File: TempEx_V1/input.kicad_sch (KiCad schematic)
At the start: 6 parts, among them J1 Conn_01x02, U1 MAX31865xTP

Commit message: WIP
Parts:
- C1, C2: footprint (none) -> Capacitor_SMD:C_0603_1608Metric_Pad1.08x0.95mm_HandSolder
- C9: value (none) -> 100n; footprint (none) -> Capacitor_SMD:C_0603_1608Metric_Pad1.08x0.95mm_HandSolder
- J1: footprint (none) -> Connector_Molex:Molex_SL_171971-0002_1x02_P2.54mm_Vertical
- R1: value (none) -> 400; footprint (none) -> Resistor_SMD:R_0201_0603Metric_Pad0.64x0.40mm_HandSolder
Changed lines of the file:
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@@
   (junction (at 134.62 96.266) (diameter 0) (color 0 0 0 0)
   )
-  (junction (at 179.578 73.66) (diameter 0) (color 0 0 0 0)
-  )
   (junction (at 204.978 100.584) (diameter 0) (color 0 0 0 0)
   )
@@
   )
   (junction (at 209.296 100.584) (diameter 0) (color 0 0 0 0)
+  )
+  (junction (at 177.038 73.66) (diameter 0) (color 0 0 0 0)
   )
   (no_connect (at 164.338 81.788))
@@
     (stroke (width 0) (type default) (color 0 0 0 0))
   )
-  (wire (pts (xy 179.578 71.628) (xy 179.578 73.66))
+  (wire (pts (xy 177.038 71.628) (xy 177.038 73.66))
     (stroke (width 0) (type default) (color 0 0 0 0))
   )
@@
     (stroke (width 0) (type default) (color 0 0 0 0))
   )
-  (wire (pts (xy 179.578 73.66) (xy 177.038 73.66))
-    (stroke (width 0) (type default) (color 0 0 0 0))
-  )
   (wire (pts (xy 197.358 81.788) (xy 200.152 81.788))
     (stroke (width 0) (type default) (color 0 0 0 0))
@@
     (stroke (width 0) (type default) (color 0 0 0 0))
   )
-  (wire (pts (xy 182.118 73.66) (xy 179.578 73.66))
+  (wire (pts (xy 177.038 73.66) (xy 182.118 73.66))
     (stroke (width 0) (type default) (color 0 0 0 0))
   )
@@
     (effects (font (size 1.27 1.27)) (justify right))
   )
-  (symbol (lib_id "power:+3.3V") (at 179.578 71.628 0) (mirror y) (unit 1)
+  (symbol (lib_id "power:+3.3V") (at 177.038 71.628 0) (mirror y)
     (in_bom yes) (on_board yes) (fields_autoplaced)
-    (property "Reference" "#PWR06" (id 0) (at 179.578 75.438 0)
-      (effects (font (size 1.27 1.27)) hide)
-    )
-    (property "Value" "" (id 1) (at 179.578 66.548 0))
-    (property "Footprint" "" (id 2) (at 179.578 71.628 0)
-      (effects (font (size 1.27 1.27)) hide)
-    )
-    (property "Datasheet" "" (id 3) (at 179.578 71.628 0)
-      (effects (font (size 1.27 1.27)) hide)
-    )
-    (pin "1")
-  )
-  (symbol (lib_id "power:GND") (at 137.16 106.934 0) (mirror y) (unit 1)
-    (in_bom yes) (on_board yes)
-    (property "Reference" "#PWR02" (id 0) (at 137.16 113.284 0)
+    (property "Reference" "#PWR024" (id 0) (at 177.038 75.438 0)
+      (effects (font (size 1.27 1.27)) hide)
+    )
+    (property "Value" "+3.3V" (id 1) (at 177.038 66.548 0))
+    (property "Footprint" "" (id 2) (at 177.038 71.628 0)
+      (effects (font (size 1.27 1.27)) hide)
+    )
+    (property "Datasheet" "" (id 3) (at 177.038 71.628 0)
+      (effects (font (size 1.27 1.27)) hide)
+    )
+    (pin "1")
+  )
+  (symbol (lib_id "power:GND") (at 137.16 106.934 0) (mirror y)
+    (in_bom yes) (on_board yes)
+    (property "Reference" "#PWR020" (id 0) (at 137.16 113.284 0)
       (effects (font (size 1.27 1.27)) hide)
     )
@@
     (pin "1")
   )
-  (symbol (lib_id "Sensor_Temperature:MAX31865xTP") (at 179.578 97.028 0) (unit 1)
+  (symbol (lib_id "Sensor_Temperature:MAX31865xTP") (at 179.578 97.028 0)
     (in_bom yes) (on_board yes) (fields_autoplaced)
     (property "Reference" "U1" (id 0) (at 174.2693 73.406 0)
@@
     (pin "9")
   )
-  (symbol (lib_id "Device:C") (at 204.978 104.394 0) (mirror y) (unit 1)
+  (symbol (lib_id "Device:C") (at 204.978 104.394 0) (mirror y)
     (in_bom yes) (on_board yes)
     (property "Reference" "C9" (id 0) (at 204.216 102.108 0)
       (effects (font (size 1.27 1.27)) (justify left))
     )
-    (property "Value" "" (id 1) (at 204.216 106.68 0)
-      (effects (font (size 1.27 1.27)) (justify left))
-    )
-    (property "Footprint" "" (id 2) (at 204.0128 108.204 0)
+    (property "Value" "100n" (id 1) (at 204.216 106.68 0)
+      (effects (font (size 1.27 1.27)) (justify left))
+    )
+    (property "Footprint" "Capacitor_SMD:C_0603_1608Metric_Pad1.08x0.95mm_HandSolder" (id 2) (at 204.0128 108.204 0)
       (effects (font (size 1.27 1.27)) hide)
     )
@@
     (pin "2")
   )
-  (symbol (lib_id "Device:C") (at 137.16 103.124 0) (mirror y) (unit 1)
+  (symbol (lib_id "Device:C") (at 137.16 103.124 0) (mirror y)
     (in_bom yes) (on_board yes)
     (property "Reference" "C1" (id 0) (at 140.716 100.838 0)
@@
       (effects (font (size 1.27 1.27)) (justify left))
     )
-    (property "Footprint" "" (id 2) (at 136.1948 106.934 0)
+    (property "Footprint" "Capacitor_SMD:C_0603_1608Metric_Pad1.08x0.95mm_HandSolder" (id 2) (at 136.1948 106.934 0)
       (effects (font (size 1.27 1.27)) hide)
     )
@@
     (pin "2")
   )
-  (symbol (lib_id "Device:C") (at 132.08 103.124 0) (mirror y) (unit 1)
+  (symbol (lib_id "Device:C") (at 132.08 103.124 0) (mirror y)
     (in_bom yes) (on_board yes)
     (property "Reference" "C2" (id 0) (at 131.572 100.838 0)
@@
       (effects (font (size 1.27 1.27)) (justify left))
     )
-    (property "Footprint" "" (id 2) (at 131.1148 106.934 0)
+    (property "Footprint" "Capacitor_SMD:C_0603_1608Metric_Pad1.08x0.95mm_HandSolder" (id 2) (at 131.1148 106.934 0)
       (effects (font (size 1.27 1.27)) hide)
     )
@@
     (pin "2")
   )
-  (symbol (lib_id "power:GND") (at 196.85 95.25 0) (mirror y) (unit 1)
-    (in_bom yes) (on_board yes)
-    (property "Reference" "#PWR026" (id 0) (at 196.85 101.6 0)
+  (symbol (lib_id "power:GND") (at 196.85 95.25 0) (mirror y)
+    (in_bom yes) (on_board yes)
+    (property "Reference" "#PWR029" (id 0) (at 196.85 101.6 0)
       (effects (font (size 1.27 1.27)) hide)
     )
@@
     (pin "1")
   )
-  (symbol (lib_id "power:GND") (at 182.118 114.808 0) (mirror y) (unit 1)
-    (in_bom yes) (on_board yes)
-    (property "Reference" "#PWR05" (id 0) (at 182.118 121.158 0)
+  (symbol (lib_id "power:PWR_FLAG") (at 182.118 73.66 0)
+    (in_bom yes) (on_board yes)
+    (property "Reference" "#FLG0104" (id 0) (at 182.118 71.755 0)
+      (effects (font (size 1.27 1.27)) hide)
+    )
+    (property "Value" "PWR_FLAG" (id 1) (at 186.563 69.977 0))
+    (property "Footprint" "" (id 2) (at 182.118 73.66 0)
+      (effects (font (size 1.27 1.27)) hide)
+    )
+    (property "Datasheet" "~" (id 3) (at 182.118 73.66 0)
+      (effects (font (size 1.27 1.27)) hide)
+    )
+    (pin "1")
+  )
+  (symbol (lib_id "power:GND") (at 182.118 114.808 0) (mirror y)
+    (in_bom yes) (on_board yes)
+    (property "Reference" "#PWR023" (id 0) (at 182.118 121.158 0)
       (effects (font (size 1.27 1.27)) hide)
     )
@@
     (pin "1")
   )
-  (symbol (lib_id "power:GNDD") (at 132.08 106.934 0) (mirror y) (unit 1)
-    (in_bom yes) (on_board yes)
-    (property "Reference" "#PWR04" (id 0) (at 132.08 113.284 0)
+  (symbol (lib_id "power:GNDD") (at 132.08 106.934 0) (mirror y)
+    (in_bom yes) (on_board yes)
+    (property "Reference" "#PWR022" (id 0) (at 132.08 113.284 0)
       (effects (font (size 1.27 1.27)) hide)
     )
@@
     (pin "1")
   )
-  (symbol (lib_id "Connector_Generic:Conn_01x02") (at 214.376 103.378 0) (unit 1)
+  (symbol (lib_id "Connector_Generic:Conn_01x02") (at 214.376 103.378 0)
     (in_bom yes) (on_board yes) (fields_autoplaced)
     (property "Reference" "J1" (id 0) (at 216.408 103.3779 0)
@@
       (effects (font (size 1.27 1.27)) (justify left))
     )
-    (property "Footprint" "" (id 2) (at 214.376 103.378 0)
+    (property "Footprint" "Connector_Molex:Molex_SL_171971-0002_1x02_P2.54mm_Vertical" (id 2) (at 214.376 103.378 0)
       (effects (font (size 1.27 1.27)) hide)
     )
@@
     (pin "2")
   )
-  (symbol (lib_id "power:GNDD") (at 177.038 114.808 0) (mirror y) (unit 1)
-    (in_bom yes) (on_board yes)
-    (property "Reference" "#PWR07" (id 0) (at 177.038 121.158 0)
+  (symbol (lib_id "power:GNDD") (at 177.038 114.808 0) (mirror y)
+    (in_bom yes) (on_board yes)
+    (property "Reference" "#PWR025" (id 0) (at 177.038 121.158 0)
       (effects (font (size 1.27 1.27)) hide)
     )
@@
     (pin "1")
   )
-  (symbol (lib_id "power:+3.3V") (at 134.62 94.234 0) (mirror y) (unit 1)
+  (symbol (lib_id "power:+3.3V") (at 134.62 94.234 0) (mirror y)
     (in_bom yes) (on_board yes) (fields_autoplaced)
-    (property "Reference" "#PWR03" (id 0) (at 134.62 98.044 0)
-      (effects (font (size 1.27 1.27)) hide)
-    )
-    (property "Value" "" (id 1) (at 134.62 88.646 0))
+    (property "Reference" "#PWR021" (id 0) (at 134.62 98.044 0)
+      (effects (font (size 1.27 1.27)) hide)
+    )
+    (property "Value" "+3.3V" (id 1) (at 134.62 88.646 0))
     (property "Footprint" "" (id 2) (at 134.62 94.234 0)
       (effects (font (size 1.27 1.27)) hide)
@@
     (pin "1")
   )
-  (symbol (lib_id "Device:R") (at 200.152 85.598 0) (unit 1)
+  (symbol (lib_id "Device:R") (at 200.152 85.598 0)
     (in_bom yes) (on_board yes)
     (property "Reference" "R1" (id 0) (at 201.93 84.582 0)
       (effects (font (size 1.27 1.27)) (justify left))
     )
-    (property "Value" "" (id 1) (at 201.676 86.614 0)
-      (effects (font (size 1.27 1.27)) (justify left))
-    )
-    (property "Footprint" "" (id 2) (at 198.374 85.598 90)
-      (effects (font (size 1.27 1.27)) hide)
-    )
+    (property "Value" "400" (id 1) (at 201.676 86.614 0)
+      (effects (font (size 1.27 1.27)) (justify left))
+    )
+    (property "Footprint" "Resistor_SMD:R_0201_0603Metric_Pad0.64x0.40mm_HandSolder" (id 2) (at 198.374 85.598 90)
+      (effects (font (size 1.27 1.27)) hide)
+    )

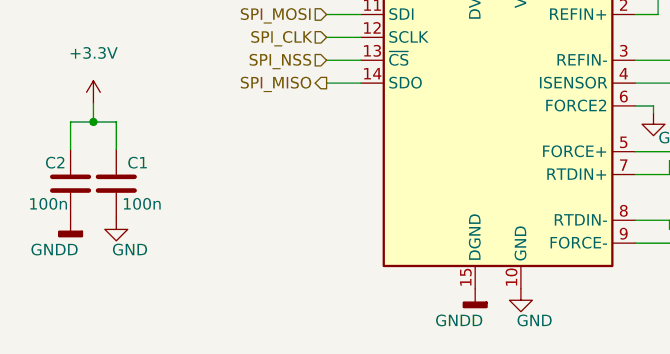
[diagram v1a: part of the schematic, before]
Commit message: GNDD Problem still unresolved
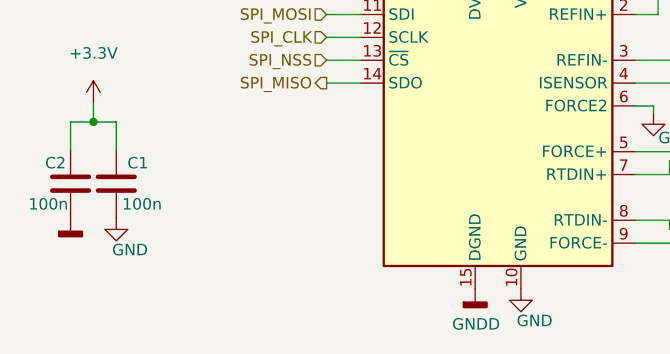
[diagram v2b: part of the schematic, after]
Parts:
- R1: footprint Resistor_SMD:R_0201_0603Metric_Pad0.64x0.40mm_HandSolder -> (none)
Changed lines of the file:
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@@
     (effects (font (size 1.27 1.27)) (justify right))
   )
-  (symbol (lib_id "power:+3.3V") (at 177.038 71.628 0) (mirror y)
-    (in_bom yes) (on_board yes) (fields_autoplaced)
-    (property "Reference" "#PWR024" (id 0) (at 177.038 75.438 0)
+  (symbol (lib_id "power:+3.3V") (at 177.038 71.628 0) (mirror y) (unit 1)
+    (in_bom yes) (on_board yes) (fields_autoplaced)
+    (property "Reference" "#PWR06" (id 0) (at 177.038 75.438 0)
       (effects (font (size 1.27 1.27)) hide)
     )
@@
     (pin "1")
   )
-  (symbol (lib_id "power:GND") (at 137.16 106.934 0) (mirror y)
-    (in_bom yes) (on_board yes)
-    (property "Reference" "#PWR020" (id 0) (at 137.16 113.284 0)
+  (symbol (lib_id "power:GNDD") (at 132.08 106.934 0) (unit 1)
+    (in_bom yes) (on_board yes)
+    (property "Reference" "#PWR022" (id 0) (at 132.08 113.284 0)
+      (effects (font (size 1.27 1.27)) hide)
+    )
+    (property "Value" "" (id 1) (at 132.1816 110.871 0))
+    (property "Footprint" "" (id 2) (at 132.08 106.934 0)
+      (effects (font (size 1.27 1.27)) hide)
+    )
+    (property "Datasheet" "" (id 3) (at 132.08 106.934 0)
+      (effects (font (size 1.27 1.27)) hide)
+    )
+    (pin "1")
+  )
+  (symbol (lib_id "power:GND") (at 137.16 106.934 0) (mirror y) (unit 1)
+    (in_bom yes) (on_board yes)
+    (property "Reference" "#PWR02" (id 0) (at 137.16 113.284 0)
       (effects (font (size 1.27 1.27)) hide)
     )
@@
     (pin "1")
   )
-  (symbol (lib_id "Sensor_Temperature:MAX31865xTP") (at 179.578 97.028 0)
+  (symbol (lib_id "Sensor_Temperature:MAX31865xTP") (at 179.578 97.028 0) (unit 1)
     (in_bom yes) (on_board yes) (fields_autoplaced)
     (property "Reference" "U1" (id 0) (at 174.2693 73.406 0)
@@
     (pin "9")
   )
-  (symbol (lib_id "Device:C") (at 204.978 104.394 0) (mirror y)
+  (symbol (lib_id "Device:C") (at 204.978 104.394 0) (mirror y) (unit 1)
     (in_bom yes) (on_board yes)
     (property "Reference" "C9" (id 0) (at 204.216 102.108 0)
@@
     (pin "2")
   )
-  (symbol (lib_id "Device:C") (at 137.16 103.124 0) (mirror y)
+  (symbol (lib_id "Device:C") (at 137.16 103.124 0) (mirror y) (unit 1)
     (in_bom yes) (on_board yes)
     (property "Reference" "C1" (id 0) (at 140.716 100.838 0)
@@
     (pin "2")
   )
-  (symbol (lib_id "Device:C") (at 132.08 103.124 0) (mirror y)
+  (symbol (lib_id "Device:C") (at 132.08 103.124 0) (mirror y) (unit 1)
     (in_bom yes) (on_board yes)
     (property "Reference" "C2" (id 0) (at 131.572 100.838 0)
@@
     (pin "2")
   )
-  (symbol (lib_id "power:GND") (at 196.85 95.25 0) (mirror y)
-    (in_bom yes) (on_board yes)
-    (property "Reference" "#PWR029" (id 0) (at 196.85 101.6 0)
+  (symbol (lib_id "power:GNDD") (at 177.038 114.808 0) (unit 1)
+    (in_bom yes) (on_board yes)
+    (property "Reference" "#PWR07" (id 0) (at 177.038 121.158 0)
+      (effects (font (size 1.27 1.27)) hide)
+    )
+    (property "Value" "GNDD" (id 1) (at 177.1396 118.745 0))
+    (property "Footprint" "" (id 2) (at 177.038 114.808 0)
+      (effects (font (size 1.27 1.27)) hide)
+    )
+    (property "Datasheet" "" (id 3) (at 177.038 114.808 0)
+      (effects (font (size 1.27 1.27)) hide)
+    )
+    (pin "1")
+  )
+  (symbol (lib_id "power:GND") (at 196.85 95.25 0) (mirror y) (unit 1)
+    (in_bom yes) (on_board yes)
+    (property "Reference" "#PWR026" (id 0) (at 196.85 101.6 0)
       (effects (font (size 1.27 1.27)) hide)
     )
@@
     (pin "1")
   )
-  (symbol (lib_id "power:PWR_FLAG") (at 182.118 73.66 0)
-    (in_bom yes) (on_board yes)
-    (property "Reference" "#FLG0104" (id 0) (at 182.118 71.755 0)
+  (symbol (lib_id "power:PWR_FLAG") (at 182.118 73.66 0) (unit 1)
+    (in_bom yes) (on_board yes)
+    (property "Reference" "#FLG0101" (id 0) (at 182.118 71.755 0)
       (effects (font (size 1.27 1.27)) hide)
     )
@@
     (pin "1")
   )
-  (symbol (lib_id "power:GND") (at 182.118 114.808 0) (mirror y)
-    (in_bom yes) (on_board yes)
-    (property "Reference" "#PWR023" (id 0) (at 182.118 121.158 0)
+  (symbol (lib_id "power:GND") (at 182.118 114.808 0) (mirror y) (unit 1)
+    (in_bom yes) (on_board yes)
+    (property "Reference" "#PWR05" (id 0) (at 182.118 121.158 0)
       (effects (font (size 1.27 1.27)) hide)
     )
@@
     (pin "1")
   )
-  (symbol (lib_id "power:GNDD") (at 132.08 106.934 0) (mirror y)
-    (in_bom yes) (on_board yes)
-    (property "Reference" "#PWR022" (id 0) (at 132.08 113.284 0)
-      (effects (font (size 1.27 1.27)) hide)
-    )
-    (property "Value" "GNDD" (id 1) (at 130.302 110.49 0))
-    (property "Footprint" "" (id 2) (at 132.08 106.934 0)
-      (effects (font (size 1.27 1.27)) hide)
-    )
-    (property "Datasheet" "" (id 3) (at 132.08 106.934 0)
-      (effects (font (size 1.27 1.27)) hide)
-    )
-    (pin "1")
-  )
-  (symbol (lib_id "Connector_Generic:Conn_01x02") (at 214.376 103.378 0)
+  (symbol (lib_id "Connector_Generic:Conn_01x02") (at 214.376 103.378 0) (unit 1)
     (in_bom yes) (on_board yes) (fields_autoplaced)
     (property "Reference" "J1" (id 0) (at 216.408 103.3779 0)
@@
     (pin "2")
   )
-  (symbol (lib_id "power:GNDD") (at 177.038 114.808 0) (mirror y)
-    (in_bom yes) (on_board yes)
-    (property "Reference" "#PWR025" (id 0) (at 177.038 121.158 0)
-      (effects (font (size 1.27 1.27)) hide)
-    )
-    (property "Value" "GNDD" (id 1) (at 175.26 118.364 0))
-    (property "Footprint" "" (id 2) (at 177.038 114.808 0)
-      (effects (font (size 1.27 1.27)) hide)
-    )
-    (property "Datasheet" "" (id 3) (at 177.038 114.808 0)
-      (effects (font (size 1.27 1.27)) hide)
-    )
-    (pin "1")
-  )
-  (symbol (lib_id "power:+3.3V") (at 134.62 94.234 0) (mirror y)
-    (in_bom yes) (on_board yes) (fields_autoplaced)
-    (property "Reference" "#PWR021" (id 0) (at 134.62 98.044 0)
+  (symbol (lib_id "power:+3.3V") (at 134.62 94.234 0) (mirror y) (unit 1)
+    (in_bom yes) (on_board yes) (fields_autoplaced)
+    (property "Reference" "#PWR03" (id 0) (at 134.62 98.044 0)
       (effects (font (size 1.27 1.27)) hide)
     )
@@
     (pin "1")
   )
-  (symbol (lib_id "Device:R") (at 200.152 85.598 0)
+  (symbol (lib_id "Device:R") (at 200.152 85.598 0) (unit 1)
     (in_bom yes) (on_board yes)
     (property "Reference" "R1" (id 0) (at 201.93 84.582 0)
@@
       (effects (font (size 1.27 1.27)) (justify left))
     )
-    (property "Footprint" "Resistor_SMD:R_0201_0603Metric_Pad0.64x0.40mm_HandSolder" (id 2) (at 198.374 85.598 90)
-      (effects (font (size 1.27 1.27)) hide)
-    )
+    (property "Footprint" "" (id 2) (at 198.374 85.598 90)
+      (effects (font (size 1.27 1.27)) hide)
+    )

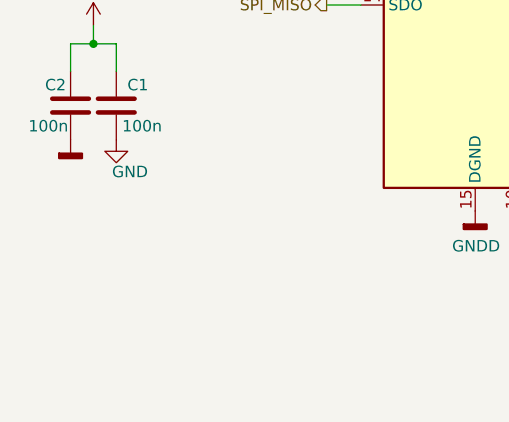
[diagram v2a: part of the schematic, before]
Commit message: Stitching missing
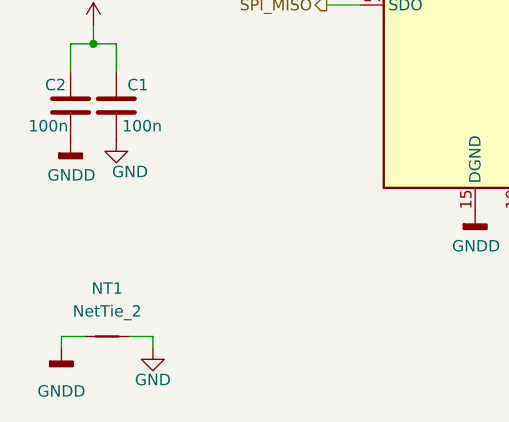
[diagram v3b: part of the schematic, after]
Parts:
- added NT1: NetTie_2, symbol Device:NetTie_2
- R1: footprint (none) -> Resistor_SMD:R_0603_1608Metric_Pad0.98x0.95mm_HandSolder
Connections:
- net GND: now also NT1.2
- net GNDD: now also NT1.1
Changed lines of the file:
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@@
+    (stroke (width 0) (type default) (color 0 0 0 0))
+  )
+  (wire (pts (xy 138.684 128.778) (xy 141.224 128.778))
     (stroke (width 0) (type default) (color 0 0 0 0))
   )
@@
     (stroke (width 0) (type default) (color 0 0 0 0))
   )
+  (wire (pts (xy 141.224 128.778) (xy 141.224 130.048))
+    (stroke (width 0) (type default) (color 0 0 0 0))
+  )
   (wire (pts (xy 194.818 81.788) (xy 197.358 81.788))
     (stroke (width 0) (type default) (color 0 0 0 0))
@@
     (stroke (width 0) (type default) (color 0 0 0 0))
   )
+  (wire (pts (xy 131.064 130.048) (xy 131.064 128.778))
+    (stroke (width 0) (type default) (color 0 0 0 0))
+  )
   (wire (pts (xy 177.038 71.628) (xy 177.038 73.66))
     (stroke (width 0) (type default) (color 0 0 0 0))
@@
   )
   (wire (pts (xy 194.818 94.488) (xy 196.85 94.488))
+    (stroke (width 0) (type default) (color 0 0 0 0))
+  )
+  (wire (pts (xy 131.064 128.778) (xy 133.604 128.778))
     (stroke (width 0) (type default) (color 0 0 0 0))
   )
@@
       (effects (font (size 1.27 1.27)) hide)
     )
-    (property "Value" "" (id 1) (at 132.1816 110.871 0))
+    (property "Value" "GNDD" (id 1) (at 132.1816 110.871 0))
     (property "Footprint" "" (id 2) (at 132.08 106.934 0)
       (effects (font (size 1.27 1.27)) hide)
@@
     (pin "1")
   )
+  (symbol (lib_id "Device:NetTie_2") (at 136.144 128.778 0) (unit 1)
+    (in_bom yes) (on_board yes) (fields_autoplaced)
+    (property "Reference" "NT1" (id 0) (at 136.144 123.444 0))
+    (property "Value" "NetTie_2" (id 1) (at 136.144 125.984 0))
+    (property "Footprint" "" (id 2) (at 136.144 128.778 0)
+      (effects (font (size 1.27 1.27)) hide)
+    )
+    (property "Datasheet" "~" (id 3) (at 136.144 128.778 0)
+      (effects (font (size 1.27 1.27)) hide)
+    )
+    (pin "1")
+    (pin "2")
+  )
   (symbol (lib_id "power:GND") (at 196.85 95.25 0) (mirror y) (unit 1)
     (in_bom yes) (on_board yes)
@@
     (pin "1")
   )
+  (symbol (lib_id "power:GNDD") (at 131.064 130.048 0) (unit 1)
+    (in_bom yes) (on_board yes) (fields_autoplaced)
+    (property "Reference" "#PWR04" (id 0) (at 131.064 136.398 0)
+      (effects (font (size 1.27 1.27)) hide)
+    )
+    (property "Value" "GNDD" (id 1) (at 131.064 134.874 0))
+    (property "Footprint" "" (id 2) (at 131.064 130.048 0)
+      (effects (font (size 1.27 1.27)) hide)
+    )
+    (property "Datasheet" "" (id 3) (at 131.064 130.048 0)
+      (effects (font (size 1.27 1.27)) hide)
+    )
+    (pin "1")
+  )
   (symbol (lib_id "Connector_Generic:Conn_01x02") (at 214.376 103.378 0) (unit 1)
     (in_bom yes) (on_board yes) (fields_autoplaced)
@@
     (pin "1")
   )
+  (symbol (lib_id "power:GND") (at 141.224 130.048 0) (unit 1)
+    (in_bom yes) (on_board yes)
+    (property "Reference" "#PWR030" (id 0) (at 141.224 136.398 0)
+      (effects (font (size 1.27 1.27)) hide)
+    )
+    (property "Value" "GND" (id 1) (at 141.224 133.604 0))
+    (property "Footprint" "" (id 2) (at 141.224 130.048 0)
+      (effects (font (size 1.27 1.27)) hide)
+    )
+    (property "Datasheet" "" (id 3) (at 141.224 130.048 0)
+      (effects (font (size 1.27 1.27)) hide)
+    )
+    (pin "1")
+  )
   (symbol (lib_id "Device:R") (at 200.152 85.598 0) (unit 1)
     (in_bom yes) (on_board yes)
@@
       (effects (font (size 1.27 1.27)) (justify left))
     )
-    (property "Footprint" "" (id 2) (at 198.374 85.598 90)
-      (effects (font (size 1.27 1.27)) hide)
-    )
+    (property "Footprint" "Resistor_SMD:R_0603_1608Metric_Pad0.98x0.95mm_HandSolder" (id 2) (at 198.374 85.598 90)
+      (effects (font (size 1.27 1.27)) hide)
+    )
